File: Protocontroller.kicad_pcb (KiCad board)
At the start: 4 copper layers, 51 x 26.4 mm, 39 parts, among them U1 AP2112K-3.3TRG1, U2 PM254-1-14-Z-8.5, U3 PM254-1-14-Z-8.5, U4 SN74AHCT245PWR, U5 SN74AHCT245PWR, U6 SN74AHCT374PWR, U8 2541WR-2x08P, U9 2541WR-2X05P

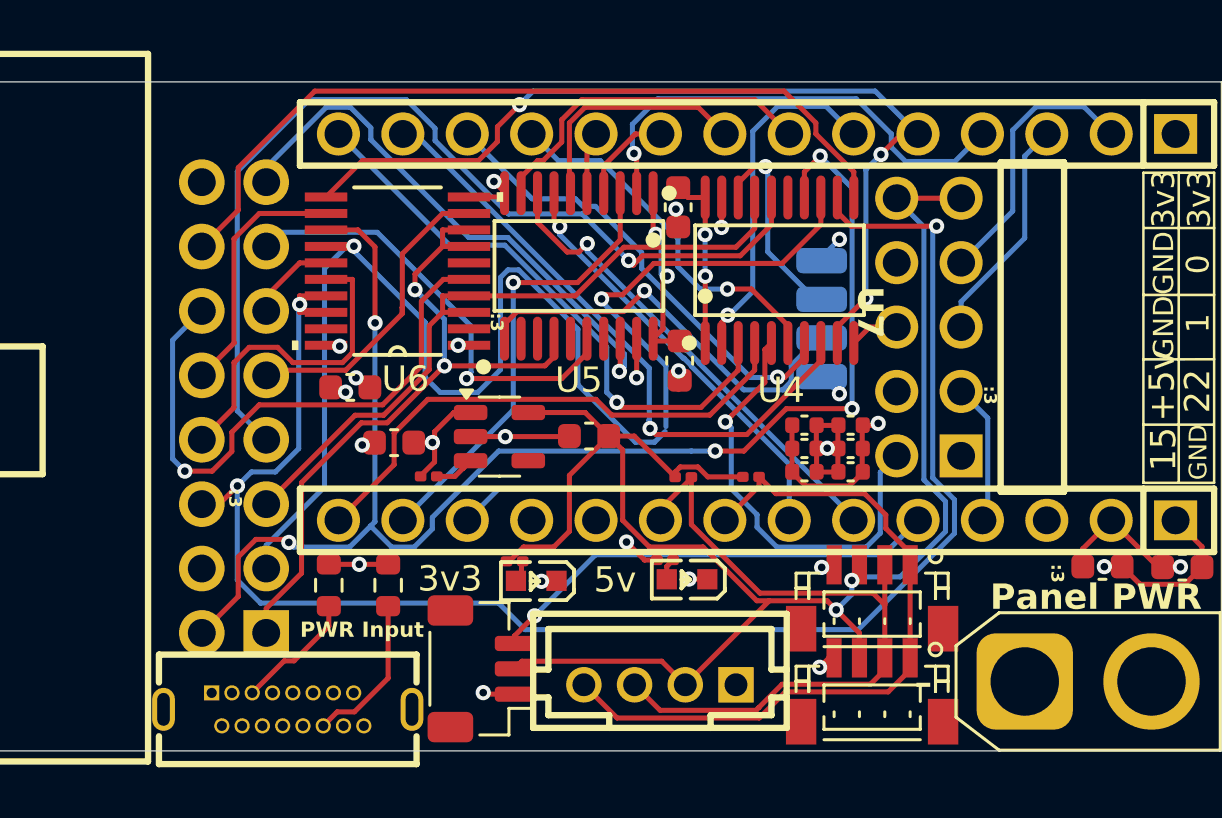
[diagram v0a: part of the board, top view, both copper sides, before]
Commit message: Fix I2C, Pathing, and improve Silkscreen
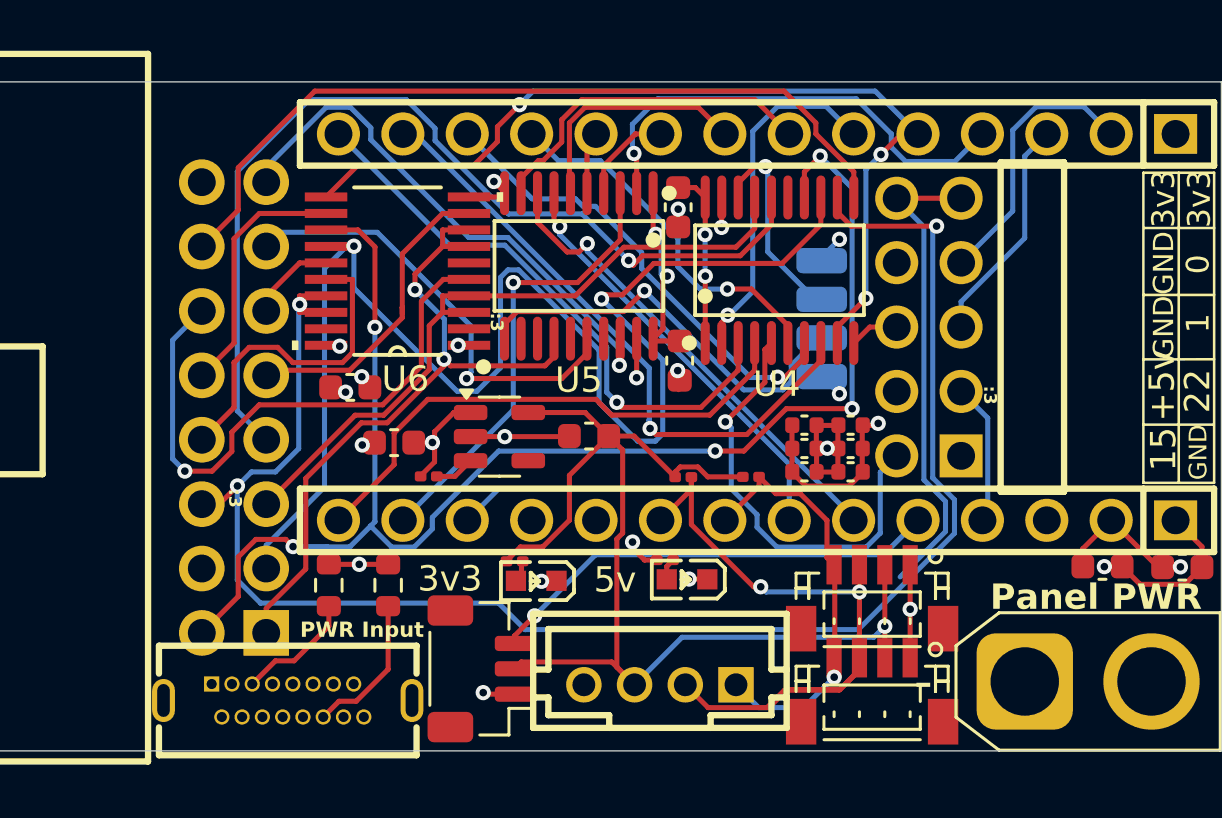
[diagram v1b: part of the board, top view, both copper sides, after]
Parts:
- C10, C11, C12, C13, C8, C9: value 22uF_0402 -> 22uF
- I2C-3: value S4B-PH-K-S_LF__SN_ -> B4B-PH-K-K(LF)(SN)
- R6, R7: value 5.1K -> 5.1K_0603
- U8: value 2541WR-2x08P -> HC-JN254-2-08-W
- moved QR 0.50 mm to (91.3, 135.5)
- moved PWR-Input1 0.35 mm to (102.1, 136.9)
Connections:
- I2C-1 pad 1: /TSCL0 -> GND
- I2C-1 pad 2: /TSDA0 -> +3.3V
- I2C-1 pad 3: +3.3V -> /TSDA0
- I2C-1 pad 4: GND -> /TSCL0
- I2C-2 pad 1: /TSCL0 -> GND
- I2C-2 pad 2: /TSDA0 -> +3.3V
- I2C-2 pad 3: +3.3V -> /TSDA0
- I2C-2 pad 4: GND -> /TSCL0
- I2C-3 pad 1: GND -> /TSCL0
- I2C-3 pad 2: +3.3V -> /TSDA0
- I2C-3 pad 3: /TSDA0 -> +3.3V
- I2C-3 pad 4: /TSCL0 -> GND
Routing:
- net /TSCL0: track 29.1 -> 16.7 mm, vias 0 -> 1
- net +3.3V: track 68.1 -> 66.2 mm, vias 2 -> 1
- net /TSDA0: track 27.4 -> 28.8 mm, vias 0 -> 2
- net +5V: track 54.8 -> 53.6 mm
- net /PANEL_OE: track 22.1 -> 21.4 mm
- net GND: track 45.3 -> 45.7 mm, vias 18 -> 17

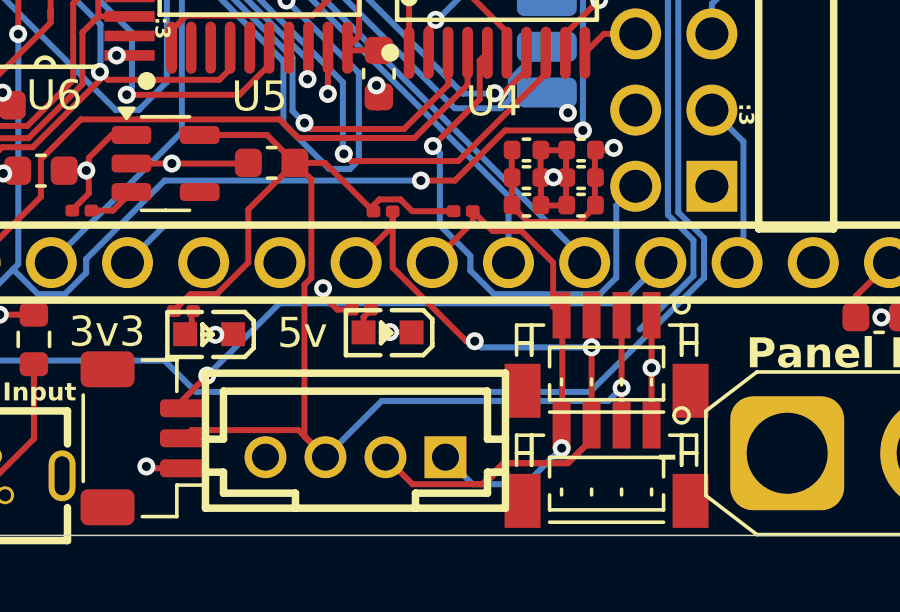
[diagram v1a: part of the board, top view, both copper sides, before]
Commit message: Fix 3v3 Trace
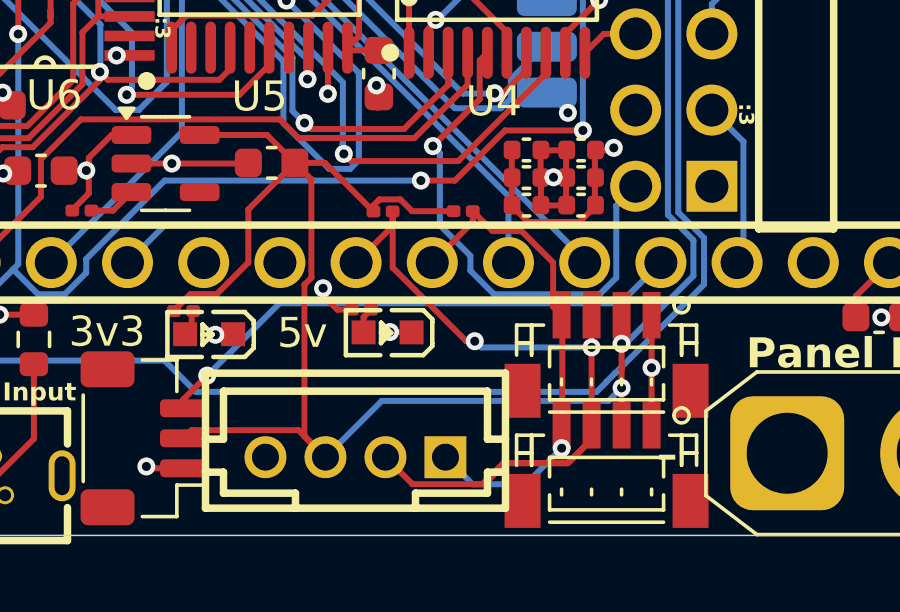
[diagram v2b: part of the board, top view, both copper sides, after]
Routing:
- net +3.3V: track 66.2 -> 67.0 mm, vias 1 -> 2
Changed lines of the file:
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@@
+	)
+	(segment
+		(start 100.15655 128.43655)
+		(end 100.1497 128.4434)
+		(width 0.2)
+		(layer "B.Cu")
+		(net 27)
 	)
 	(segment
 		(start 111.5029 134.1048)
-		(end 124.6417 134.1048)
-		(width 0.2)
-		(layer "B.Cu")
-		(net 27)
-	)
-	(segment
-		(start 124.6417 134.1048)
-		(end 128.4383 130.3082)
+		(end 124.8552 134.1048)
+		(width 0.2)
+		(layer "B.Cu")
+		(net 27)
+	)
+	(segment
+		(start 127.5801 118.345459)
+		(end 127.733603 118.191956)
+		(width 0.2)
+		(layer "B.Cu")
+		(net 27)
+	)
+	(segment
+		(start 125.491 133.469)
+		(end 128.4383 130.5217)
+		(width 0.2)
+		(layer "B.Cu")
+		(net 27)
+	)
+	(segment
+		(start 127.733603 118.191956)
+		(end 127.733603 118.188557)
+		(width 0.2)
+		(layer "B.Cu")
+		(net 27)
+	)
+	(segment
+		(start 102.573597 121.316503)
+		(end 102.6101 121.28)
+		(width 0.2)
+		(layer "B.Cu")
+		(net 27)
+	)
+	(segment
+		(start 100.7081 127.885)
+		(end 101.6543 127.885)
+		(width 0.2)
+		(layer "B.Cu")
+		(net 27)
+	)
+	(segment
+		(start 100.1497 132.1427)
+		(end 101.0664 133.0594)
+		(width 0.2)
+		(layer "B.Cu")
+		(net 27)
+	)
+	(segment
+		(start 124.8552 134.1048)
+		(end 125.189 133.771)
+		(width 0.2)
+		(layer "B.Cu")
+		(net 27)
+	)
+	(segment
+		(start 128.4383 128.9773)
+		(end 127.5801 128.1191)
 		(width 0.2)
 		(layer "B.Cu")
@@
 	)
 	(segment
+		(start 100.15655 128.43655)
+		(end 100.7081 127.885)
+		(width 0.2)
+		(layer "B.Cu")
+		(net 27)
+	)
+	(segment
+		(start 125.189 133.762479)
+		(end 125.482479 133.469)
+		(width 0.2)
+		(layer "B.Cu")
+		(net 27)
+	)
+	(segment
+		(start 102.573597 126.965703)
+		(end 102.573597 121.316503)
+		(width 0.2)
+		(layer "B.Cu")
+		(net 27)
+	)
+	(segment
+		(start 125.482479 133.469)
+		(end 125.491 133.469)
+		(width 0.2)
+		(layer "B.Cu")
+		(net 27)
+	)
+	(segment
+		(start 127.5801 128.1191)
+		(end 127.5801 118.345459)
+		(width 0.2)
+		(layer "B.Cu")
+		(net 27)
+	)
+	(segment
+		(start 125.189 133.771)
+		(end 125.189 133.762479)
+		(width 0.2)
+		(layer "B.Cu")
+		(net 27)
+	)
+	(segment
+		(start 128.4383 130.5217)
+		(end 128.4383 128.9773)
+		(width 0.2)
+		(layer "B.Cu")
+		(net 27)
+	)
+	(segment
+		(start 110.4575 133.0594)
+		(end 111.5029 134.1048)
+		(width 0.2)
+		(layer "B.Cu")
+		(net 27)
+	)
+	(segment
+		(start 101.6543 127.885)
+		(end 102.573597 126.965703)
+		(width 0.2)
+		(layer "B.Cu")
+		(net 27)
+	)
+	(segment
 		(start 100.1497 128.4434)
 		(end 100.1497 132.1427)
-		(width 0.2)
-		(layer "B.Cu")
-		(net 27)
-	)
-	(segment
-		(start 127.5801 128.1191)
-		(end 127.5801 118.345459)
-		(width 0.2)
-		(layer "B.Cu")
-		(net 27)
-	)
-	(segment
-		(start 102.573597 121.316503)
-		(end 102.6101 121.28)
-		(width 0.2)
-		(layer "B.Cu")
-		(net 27)
-	)
-	(segment
-		(start 100.7081 127.885)
-		(end 101.6543 127.885)
-		(width 0.2)
-		(layer "B.Cu")
-		(net 27)
-	)
-	(segment
-		(start 100.1497 132.1427)
-		(end 101.0664 133.0594)
-		(width 0.2)
-		(layer "B.Cu")
-		(net 27)
-	)
-	(segment
-		(start 127.733603 118.191956)
-		(end 127.733603 118.188557)
-		(width 0.2)
-		(layer "B.Cu")
-		(net 27)
-	)
-	(segment
-		(start 110.4575 133.0594)
-		(end 111.5029 134.1048)
-		(width 0.2)
-		(layer "B.Cu")
-		(net 27)
-	)
-	(segment
-		(start 100.15655 128.43655)
-		(end 100.7081 127.885)
-		(width 0.2)
-		(layer "B.Cu")
-		(net 27)
-	)
-	(segment
-		(start 102.573597 126.965703)
-		(end 102.573597 121.316503)
-		(width 0.2)
-		(layer "B.Cu")
-		(net 27)
-	)
-	(segment
-		(start 100.15655 128.43655)
-		(end 100.1497 128.4434)
-		(width 0.2)
-		(layer "B.Cu")
-		(net 27)
-	)
-	(segment
-		(start 127.5801 118.345459)
-		(end 127.733603 118.191956)
-		(width 0.2)
-		(layer "B.Cu")
-		(net 27)
-	)
-	(segment
-		(start 128.4383 128.9773)
-		(end 127.5801 128.1191)
-		(width 0.2)
-		(layer "B.Cu")
-		(net 27)
-	)
-	(segment
-		(start 101.6543 127.885)
-		(end 102.573597 126.965703)
-		(width 0.2)
-		(layer "B.Cu")
-		(net 27)
-	)
-	(segment
-		(start 128.4383 130.3082)
-		(end 128.4383 128.9773)
 		(width 0.2)
 		(layer "B.Cu")
@@
 	)
 	(segment
+		(start 125.69 133.35)
+		(end 125.69 133.97)
+		(width 0.2)
+		(layer "F.Cu")
+		(net 48)
+	)
+	(segment
 		(start 125.69 131.5475)
-		(end 125.69 133.97)
+		(end 125.69 133.35)
 		(width 0.2)
 		(layer "F.Cu")
@@
 		(width 0.2)
 		(layer "F.Cu")
+		(net 48)
+	)
+	(via
+		(at 125.69 132.5)
+		(size 0.6)
+		(drill 0.3)
+		(layers "F.Cu" "B.Cu")
 		(net 48)
 	)
@@
 	)
 	(segment
-		(start 126.2959 132.024)
-		(end 128.085 130.2349)
+		(start 126.16 117.144)
+		(end 126.16 117.09)
 		(width 0.2)
 		(layer "B.Cu")
@@
 	)
 	(segment
+		(start 117.6942 134.4058)
+		(end 115.82 136.28)
+		(width 0.2)
+		(layer "B.Cu")
+		(net 48)
+	)
+	(segment
+		(start 127.2345 118.2185)
+		(end 126.16 117.144)
+		(width 0.2)
+		(layer "B.Cu")
+		(net 48)
+	)
+	(segment
+		(start 128.085 130.2349)
+		(end 128.085 129.0505)
+		(width 0.2)
+		(layer "B.Cu")
+		(net 48)
+	)
+	(segment
+		(start 125.8199 132.5)
+		(end 128.085 130.2349)
+		(width 0.2)
+		(layer "B.Cu")
+		(net 48)
+	)
+	(segment
+		(start 128.085 129.0505)
+		(end 127.2345 128.2)
+		(width 0.2)
+		(layer "B.Cu")
+		(net 48)
+	)
+	(segment
 		(start 127.2345 128.2)
 		(end 127.2345 118.2185)
@@
 	)
 	(segment
-		(start 126.16 117.144)
-		(end 126.16 117.09)
-		(width 0.2)
-		(layer "B.Cu")
-		(net 48)
-	)
-	(segment
-		(start 117.6942 134.4058)
-		(end 115.82 136.28)
-		(width 0.2)
-		(layer "B.Cu")
-		(net 48)
-	)
-	(segment
-		(start 127.2345 118.2185)
-		(end 126.16 117.144)
-		(width 0.2)
-		(layer "B.Cu")
-		(net 48)
-	)
-	(segment
-		(start 128.085 129.0505)
-		(end 127.2345 128.2)
-		(width 0.2)
-		(layer "B.Cu")
-		(net 48)
-	)
-	(segment
-		(start 128.085 130.2349)
-		(end 128.085 129.0505)
-		(width 0.2)
-		(layer "B.Cu")
+		(start 125.69 132.5)
+		(end 125.8199 132.5)
+		(width 0.2)
+		(layer "B.Cu")

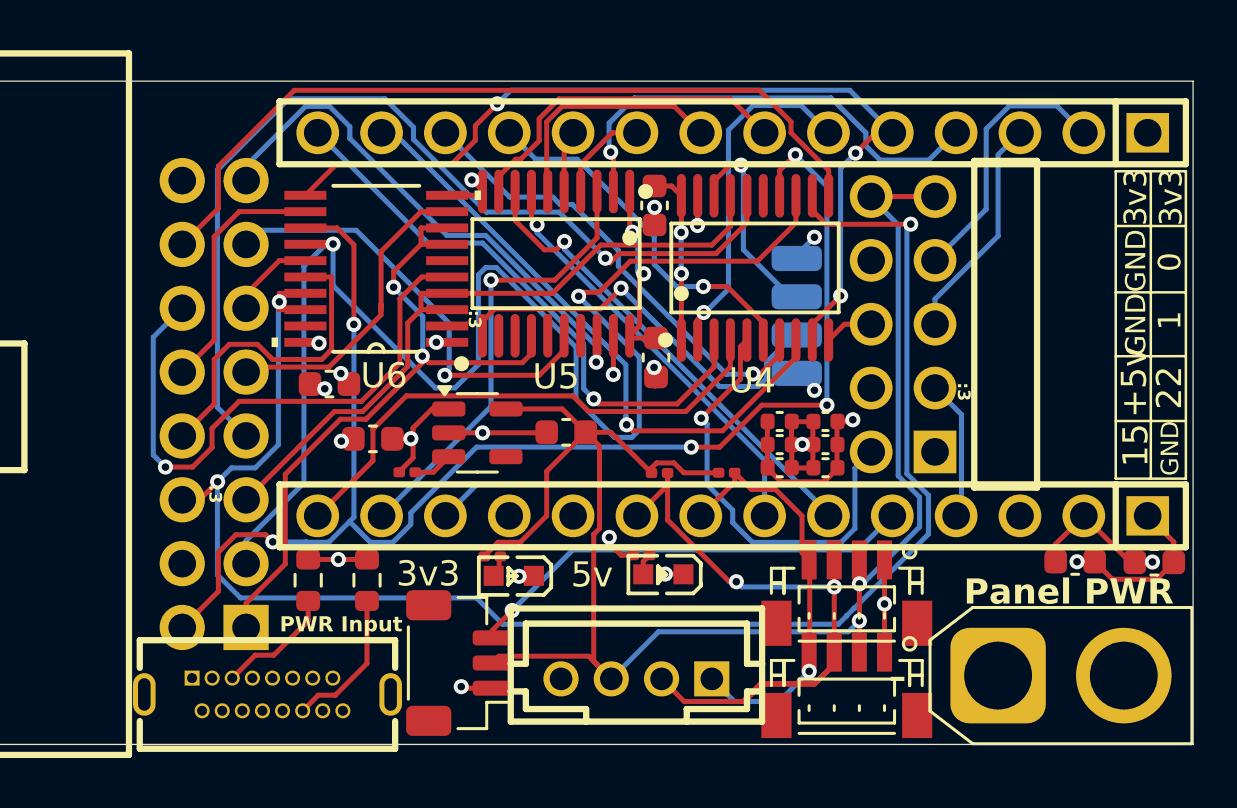
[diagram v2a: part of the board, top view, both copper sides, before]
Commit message: Remove WS35 Support, Adjust Traces, Fix issue with Panel out not actually being connected to anything
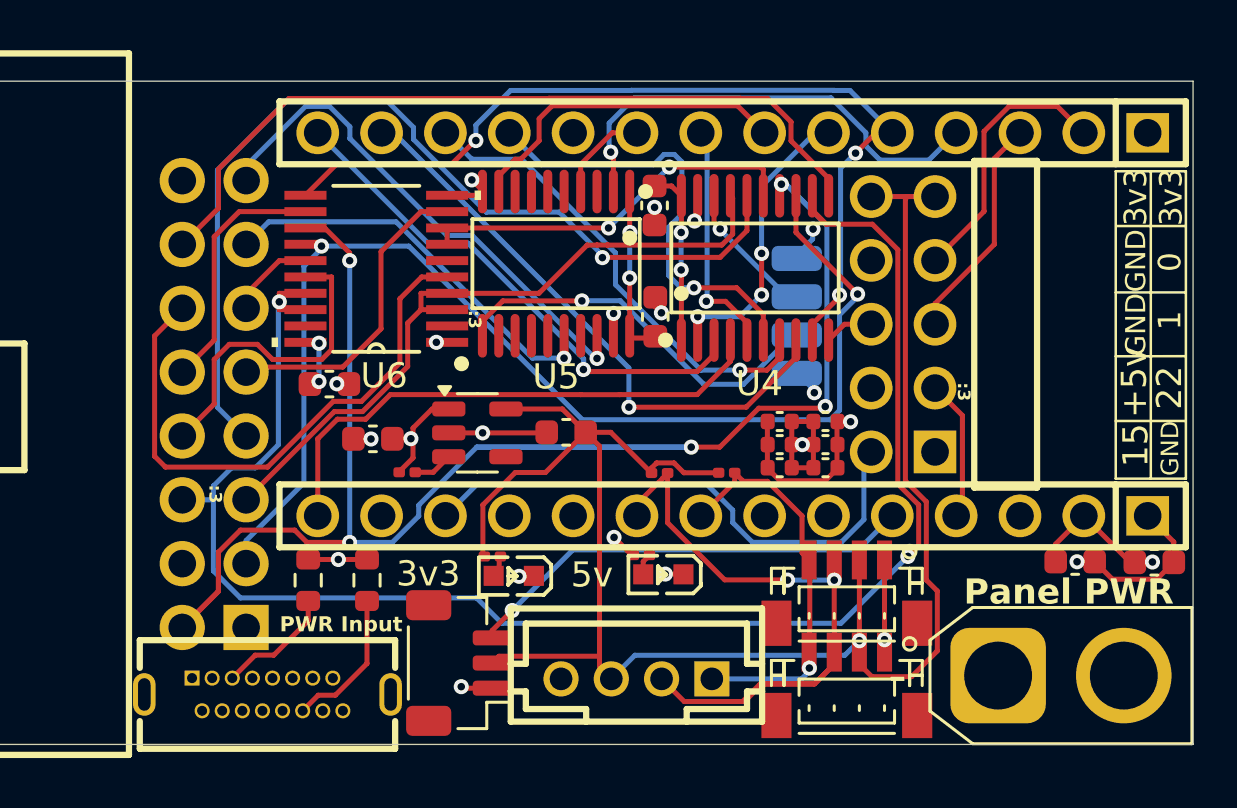
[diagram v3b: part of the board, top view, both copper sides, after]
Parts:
- moved C5 1.62 mm to (117.6, 121.9), turned to -90 degrees
- moved Logo 1.25 mm to (134.8, 122.1)
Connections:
- net /BUFFER_CLK_A3_7 renamed /BUFFER_CLK
- net /BUFFER_OE_A1_2 renamed /BUFFER_OE
- net /FLEXIO_MOSI_A8_5 renamed /FLEXIO_MOSI
- Panel-PWR1 pad 1: (no net) -> GND
- Panel-PWR1 pad 2: (no net) -> +5V
- U2 pad 10: /A4_8 -> unconnected-(U2-Pad10)
- U2 pad 8: /BUFFER_R1_A5_6 -> /BUFFER_R1
- U3 pad 13: /A2_14 -> unconnected-(U3-Pad13)
- U3 pad 6: /A7_21 -> unconnected-(U3-Pad6)
- U3 pad 7: /A6_20 -> unconnected-(U3-Pad7)
- U4 pad 15: /SPWM1 -> Net-(U4-B4)
- U4 pad 5: /TPWM1 -> /BUFFER_R1
- U5 pad 14: /PANEL_R1 -> unconnected-(U5-B5-Pad14)
- U5 pad 3: /A2_14 -> unconnected-(U5-A2-Pad3)
- U5 pad 5: /A4_8 -> unconnected-(U5-A4-Pad5)
- U5 pad 6: /BUFFER_R1_A5_6 -> unconnected-(U5-A5-Pad6)
- U5 pad 7: /A6_20 -> unconnected-(U5-A6-Pad7)
- U5 pad 8: /A7_21 -> unconnected-(U5-A7-Pad8)
- U6 pad 7: /PANEL_R1 -> Net-(U4-B4)
- U6 pad 8: /PANEL_R1 -> Net-(U4-B4)
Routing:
- net /PANEL_R1: track 27.7 -> 0.00 mm, vias 2 -> 0
- net /A7_21: track 19.0 -> 0.00 mm, vias 1 -> 0
- net /A2_14: track 17.9 -> 0.00 mm, vias 1 -> 0
- net /A6_20: track 16.7 -> 0.00 mm, vias 1 -> 0
- net Net-(U4-B4): track 0.00 -> 15.3 mm, vias 0 -> 2
- net /PANEL_G1: track 57.1 -> 69.3 mm
- net /BUFFER_R1: track 0.00 -> 9.86 mm, vias 0 -> 1
- net /BUFFER_R1_A5_6: track 9.61 -> 0.00 mm
- net /PANEL_B1: track 56.5 -> 48.0 mm
- net /TPWM1: track 28.2 -> 21.6 mm, vias 1 -> 0
- net +3.3V: track 67.0 -> 72.0 mm, vias 2 -> 1
- net +5V: track 53.6 -> 50.2 mm
- net /BUFFER_G1: track 14.6 -> 17.9 mm
- net /APA_CLK: track 8.17 -> 5.61 mm
- net /A4_8: track 2.48 -> 0.00 mm
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
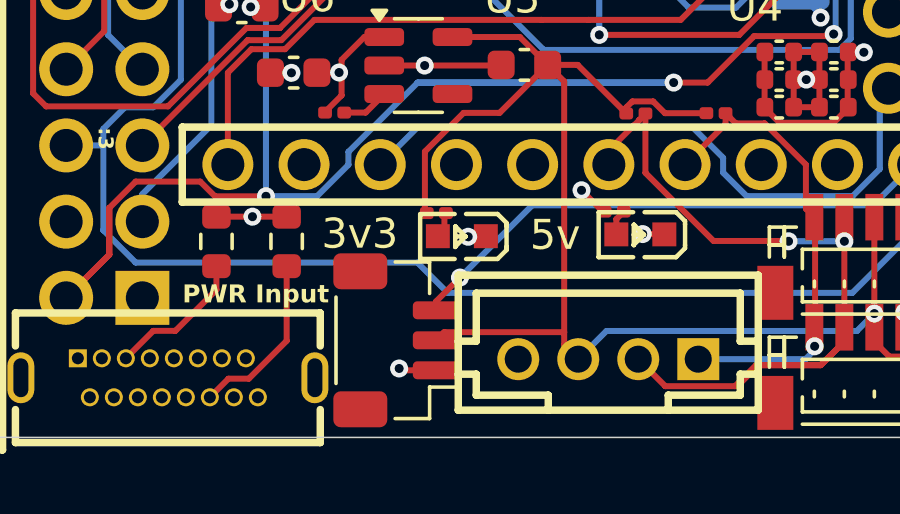
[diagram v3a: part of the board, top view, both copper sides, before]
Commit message: Fix 3v3 Regulator having bad Rotation, Fix issue of Mic and Led's being replaced when updating from schematic.
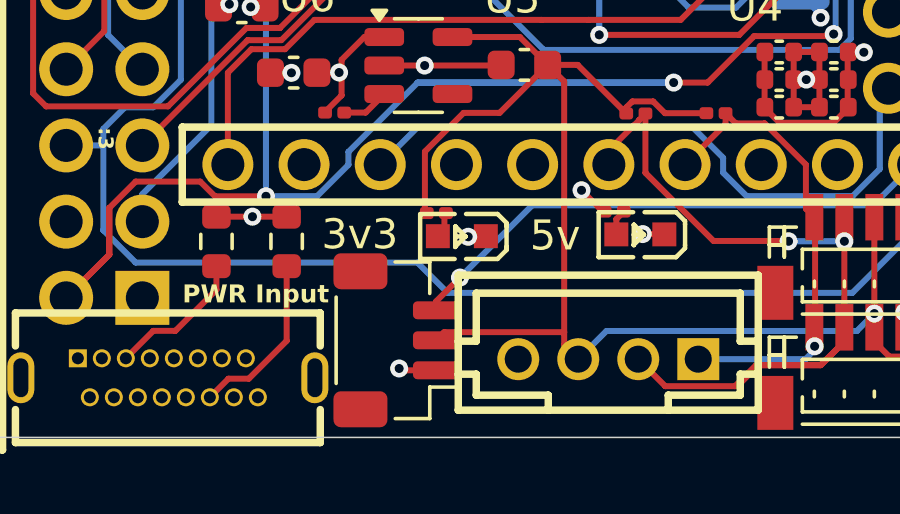
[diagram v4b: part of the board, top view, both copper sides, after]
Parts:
- renumbered U7 to APA102-Pad1, U9 to IO1
